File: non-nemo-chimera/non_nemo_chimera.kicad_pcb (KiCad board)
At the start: 2 copper layers, 273.7 x 107 mm, 92 parts, among them J1 Conn_BAT, J2 Conn_BAT, X1 5.5mm, X10 5.5mm, X2 5.5mm, X3 5.5mm, X4 5.5mm, X5 5.5mm, X6 5.5mm, X7 5.5mm, X8 5.5mm, X9 5.5mm

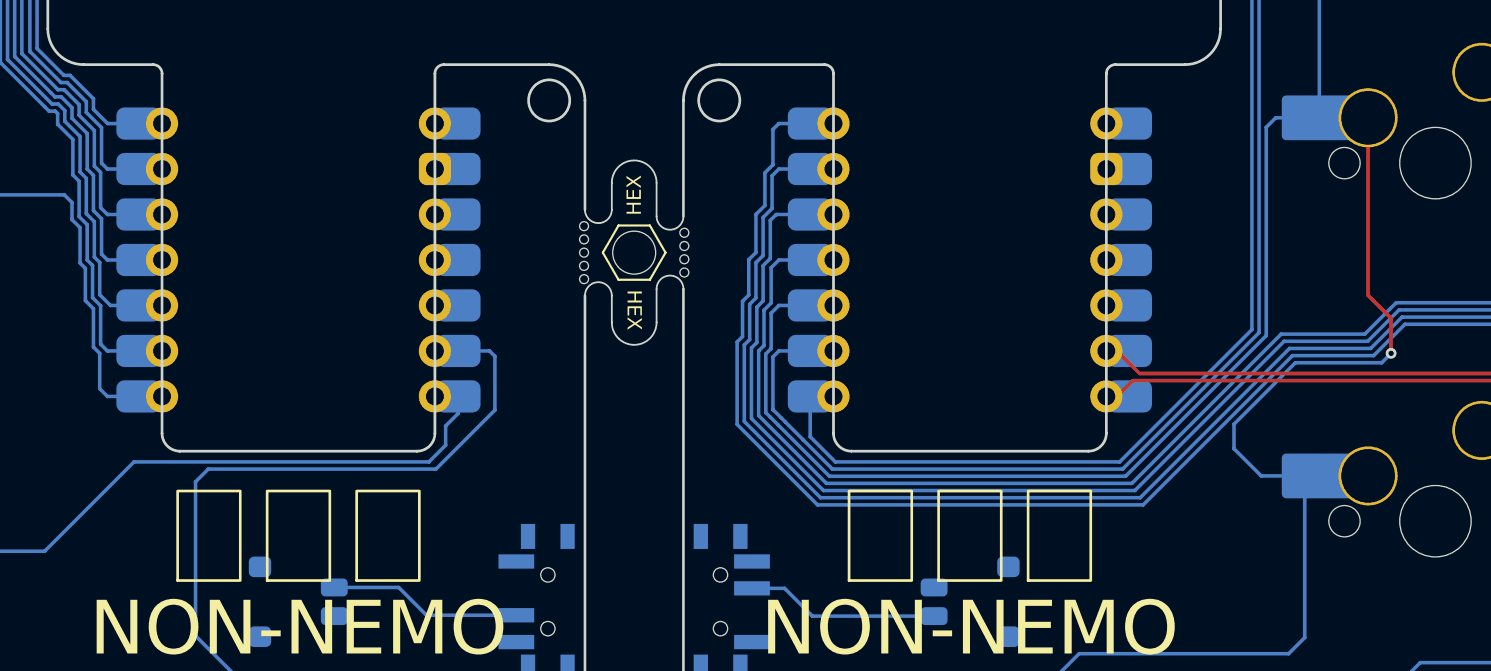
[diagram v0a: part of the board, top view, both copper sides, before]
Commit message: reset switch (#6)
* added reset switch

* Low Profile

pogopin and reset button

* MX Profile

pogopin and reset switch

* MX Profile PCB

* Chimera

pogopin and reset switch

* version

* updated README.md
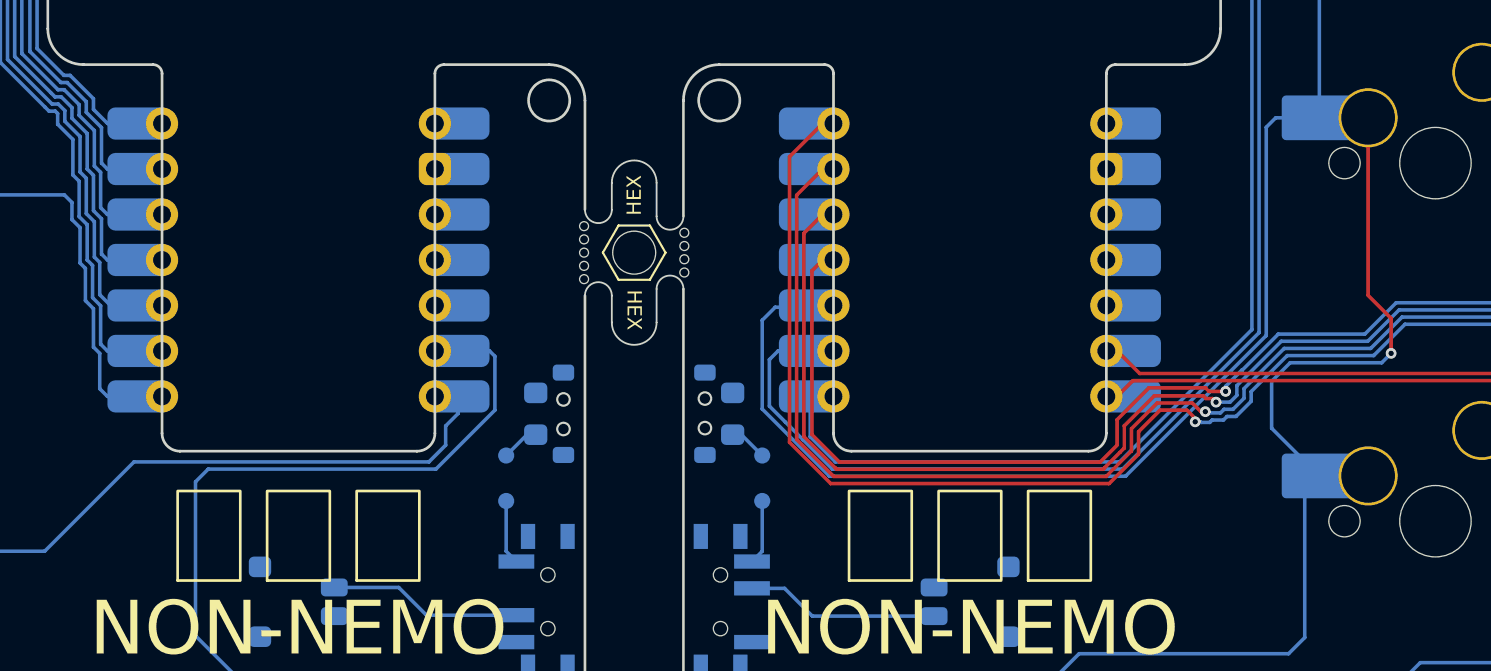
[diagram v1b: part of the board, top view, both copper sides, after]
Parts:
- added J3: Conn_BAT, TB2086_MISC:Molex_Pico-EZmate_78171-0002_1x02-1MP_P1.20mm_HandSolder, F.Cu at (136.0, 104.5)
- added J4: Conn_BAT, TB2086_MISC:Molex_Pico-EZmate_78171-0002_1x02-1MP_P1.20mm_HandSolder, F.Cu at (173.5, 104.5)
- added RSW1: SMT 2X4X3.5MM Tactile Tact Push Button, TB2086_SMD:SMT 2X4X3.5MM Tactile Tact Push Button, F.Cu at (150.8, 94.0)
- added RSW2: SMT 2X4X3.5MM Tactile Tact Push Button, TB2086_SMD:SMT 2X4X3.5MM Tactile Tact Push Button, F.Cu at (158.7, 94.0)
- J1, J2: value Conn_BAT -> Conn_01x02; footprint TB2086_MISC:Molex_Pico-EZmate_78171-0002_1x02-1MP_P1.20mm_HandSolder -> TB2086_MISC:Tag_Pogopin_1x02_P2.54mm
- MCU1, MCU2: footprint TB2086_G_MCU:Xiao_nRF52840_edgecut -> TB2086_MCU:Xiao_nRF52840_edgecut
- S16, S17, S18: footprint TB2086_KEYSWITCH:SW_choc_v1_v2_HS_1u -> TB2086_KEYSWITCH:SW_MX_HS_1u
- S31, S32, S33: value SW_MX_HS -> SW_CHOC_HS; footprint TB2086_KEYSWITCH:SW_MX_HS_1u -> TB2086_KEYSWITCH:SW_choc_v1_v2_HS_1u
- S34, S35, S36: value SW_MX_HS -> SW_CHOC_HS
- moved D16 195.4 mm to (287.0, 100.0), turned to 90 degrees
- moved S16 180.8 mm to (279.5, 100.0)
- moved D17 178.8 mm to (287.0, 80.0), turned to 90 degrees
- moved X5 169.9 mm to (30.0, 42.5), turned to 90 degrees
- moved X7 169.5 mm to (279.5, 42.5)
- moved D18 165.4 mm to (287.0, 60.0), turned to 90 degrees
- moved S17 164.9 mm to (279.5, 80.0)
- moved S18 152.7 mm to (279.5, 60.0)
- moved D31 116.1 mm to (92.5, 119.0), turned to -90 degrees
- moved D32 102.2 mm to (112.5, 119.0), turned to -90 degrees
- moved S31 101.9 mm to (100.0, 122.0)
- moved D33 95.0 mm to (132.5, 119.0), turned to -90 degrees
- moved S32 89.9 mm to (120.0, 122.0)
- moved S33 85.9 mm to (140.0, 122.0)
- moved X6 80.0 mm to (110.0, 42.5)
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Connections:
- D16 pad 1: row_thumb -> row_bottom_r
- D17 pad 1: row_thumb -> row_home_r
- D18 pad 1: row_thumb -> row_top_r
- D31 pad 1: row_bottom_r -> row_thumb
- D32 pad 1: row_home_r -> row_thumb
- D33 pad 1: row_top_r -> row_thumb
- J1 pad 1: GND -> BAT
- J1 pad 2: Net-(J1-Pin_2) -> RST
- J2 pad 1: GND -> BAT_r
- J2 pad 2: Net-(J2-Pin_2) -> RST_r
- S16 pad 2: col_middle -> col_pinky_r
- S17 pad 2: col_index -> col_pinky_r
- S18 pad 2: col_inner -> col_pinky_r
- S19 pad 2: col_pinky_r -> col_ring_r
- S20 pad 2: col_pinky_r -> col_ring_r
- S21 pad 2: col_pinky_r -> col_ring_r
- S22 pad 2: col_ring_r -> col_middle_r
- S23 pad 2: col_ring_r -> col_middle_r
- S24 pad 2: col_ring_r -> col_middle_r
- S25 pad 2: col_middle_r -> col_index_r
- S26 pad 2: col_middle_r -> col_index_r
- S27 pad 2: col_middle_r -> col_index_r
- S28 pad 2: col_index_r -> col_inner_r
- S29 pad 2: col_index_r -> col_inner_r
- S30 pad 2: col_index_r -> col_inner_r
- S31 pad 2: col_inner_r -> col_middle
- S32 pad 2: col_inner_r -> col_index
- S33 pad 2: col_inner_r -> col_inner
- SW_SPDT1 pad : (no net) -> GND
- SW_SPDT1 pad 2: Net-(J1-Pin_2) -> Net-(J3-Pin_2)
- SW_SPDT2 pad : (no net) -> GND
- SW_SPDT2 pad 2: Net-(J2-Pin_2) -> Net-(J4-Pin_2)
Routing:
- net Net-(J4-Pin_2): track 0.00 -> 10.8 mm
- net Net-(J2-Pin_2): track 10.8 -> 0.00 mm
- net Net-(J3-Pin_2): track 0.00 -> 10.8 mm
- net Net-(J1-Pin_2): track 10.8 -> 0.00 mm
- net col_index_r: track 165.6 -> 161.4 mm, vias 0 -> 1
- net col_middle_r: track 190.8 -> 186.8 mm, vias 0 -> 1
- net col_ring_r: track 164.4 -> 160.7 mm, vias 0 -> 1
- net BAT_r: track 0.00 -> 3.62 mm
- net BAT: track 0.00 -> 3.62 mm
- net col_pinky_r: track 185.6 -> 182.0 mm, vias 0 -> 1
- net col_inner_r: track 155.3 -> 152.0 mm
- net RST_r: track 0.00 -> 2.13 mm
- net RST: track 0.00 -> 2.13 mm
- net Net-(D32-A): track 4.20 -> 5.14 mm
- net Net-(D31-A): track 4.20 -> 5.14 mm
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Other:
- board text added: "B+"
- board text added: "Non Nemo 0.2.0"
- board text added: "RST"
- board text removed: "Non Nemo 0.1.6"

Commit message: fixed footprint layer for Chimera
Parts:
- D1, D10, D11, D12, D13, D14, D15, D16, D17, D18, D19, D2, D20, D21, D22, D23, D24, D25, D26, D27, D28, D29, D3, D30, D31, D32, D33, D34, D35, D36, D4, D5, D6, D7, D8, D9: value D -> 1N4148W; footprint TB2086_SMD:TB2086_SMD_D3_SMD -> TB2086_SMD:D3_SMD; moved to B.Cu
- J1, J2, J3, J4, LOGO2, LOGO4, MCU1, MCU2, RSW1, RSW2, S1, S10, S11, S12, S13, S14, S15, S16, S17, S18, S19, S2, S20, S21, S22, S23, S24, S25, S26, S27, S28, S29, S3, S30, S31, S32, S33, S34, S35, S36, S4, S5, S6, S7, S8, S9, SW_SPDT1, SW_SPDT2, X1, X10, X2, X3, X4, X5, X6, X7, X8, X9: moved to B.Cu
